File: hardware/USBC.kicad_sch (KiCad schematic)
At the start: 16 parts, among them J20 USB_C_Receptacle_USB2.0_16P, U11 CDSOT236-0504C, U33 USBLC6-2P6, U8 CP2102N-A02-GQFN20

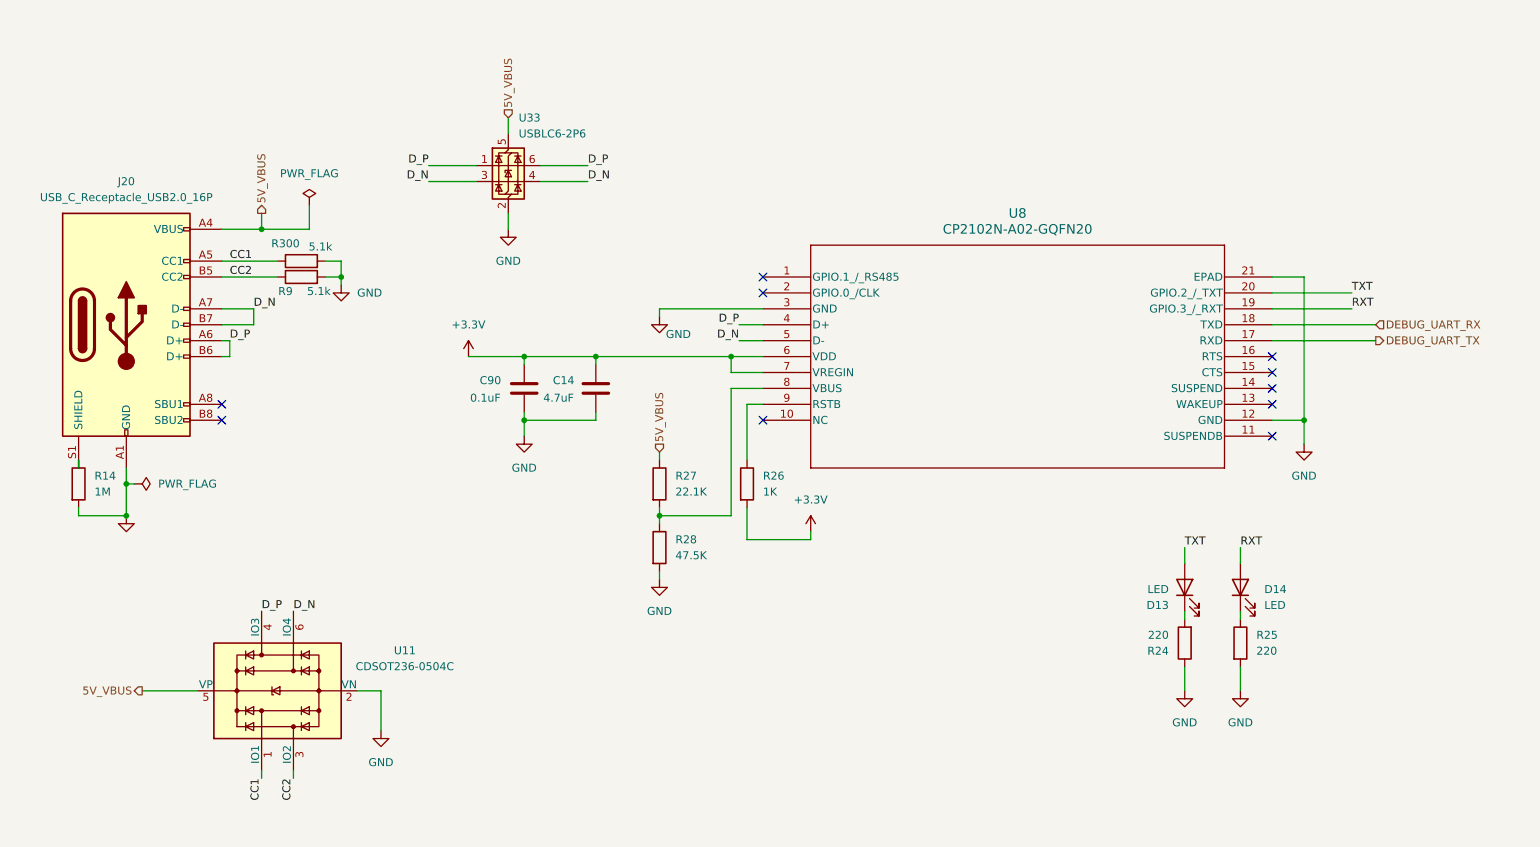
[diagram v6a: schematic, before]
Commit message: updated major symbol and footprints
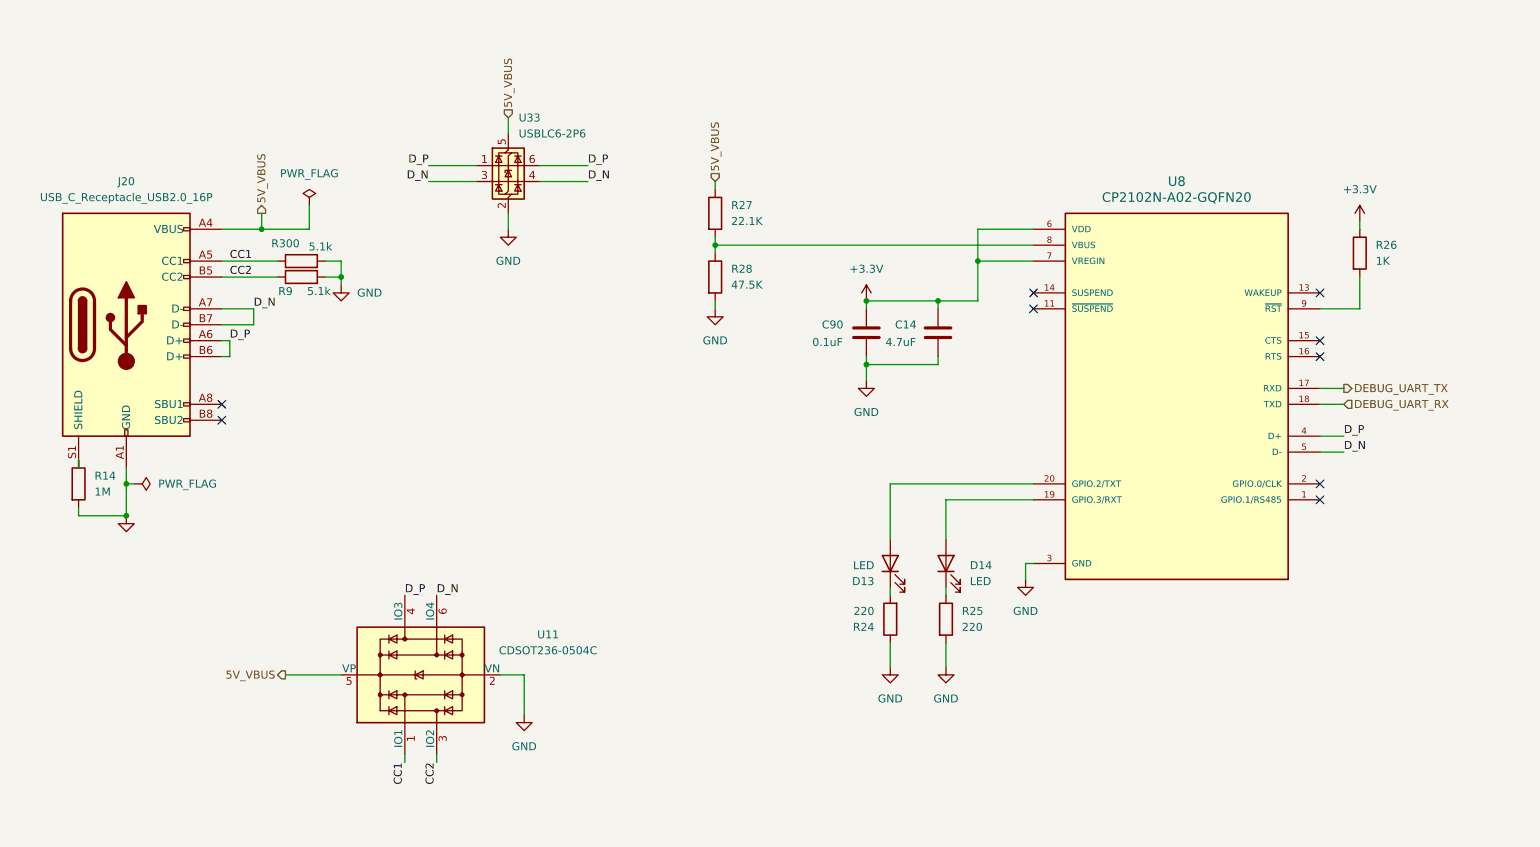
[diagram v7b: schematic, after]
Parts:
- U8: footprint Custom_Parts:QFN50P400X400X80-25N -> pyronet_footprints:SILABS_CP2102N-A02-GQFN20R; symbol 2026-02-15_23-19-28:CP2102N-A02-GQFN20 -> pyronet_symbols:CP2102N-A02-GQFN20R; Availability (none) -> In Stock; Check_prices (none) -> https://www.snapeda.com/parts/CP2102N-A02-GQFN20R/Silicon+L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; Description_1 (none) -> USB Bridge, USB to UART USB 2.0 UART Interface 20-QFN (3x3); MANUFACTURER (none) -> SILICON LABS; MAXIMUM_PACKAGE_HIEGHT (none) -> 0.8mm; MF (none) -> Silicon Labs; MP (none) -> CP2102N-A02-GQFN20R; PARTREV (none) -> 1.3; Package (none) -> WFQFN-20 Silicon Labs; Price (none) -> None; STANDARD (none) -> Manufacturer Recommendations; SnapEDA_Link (none) -> https://www.snapeda.com/parts/CP2102N-A02-GQFN20R/Silicon+L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
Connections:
- net +3.3V: now also R26.1; no longer R26.2
- net at U8.9 (~{RST}): now also R26.2; no longer R26.1
- net RXT: no longer names the net of D14.2 (A), U8.19 (GPIO.3/RXT)
- net TXT: no longer names the net of D13.2 (A), U8.20 (GPIO.2/TXT)
- no-connect marks 10 -> 9
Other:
- moved on the sheet: C14, C90, D13, D14, R24, R25, R26, R27, R28, U11

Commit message: updated 5V power and pin
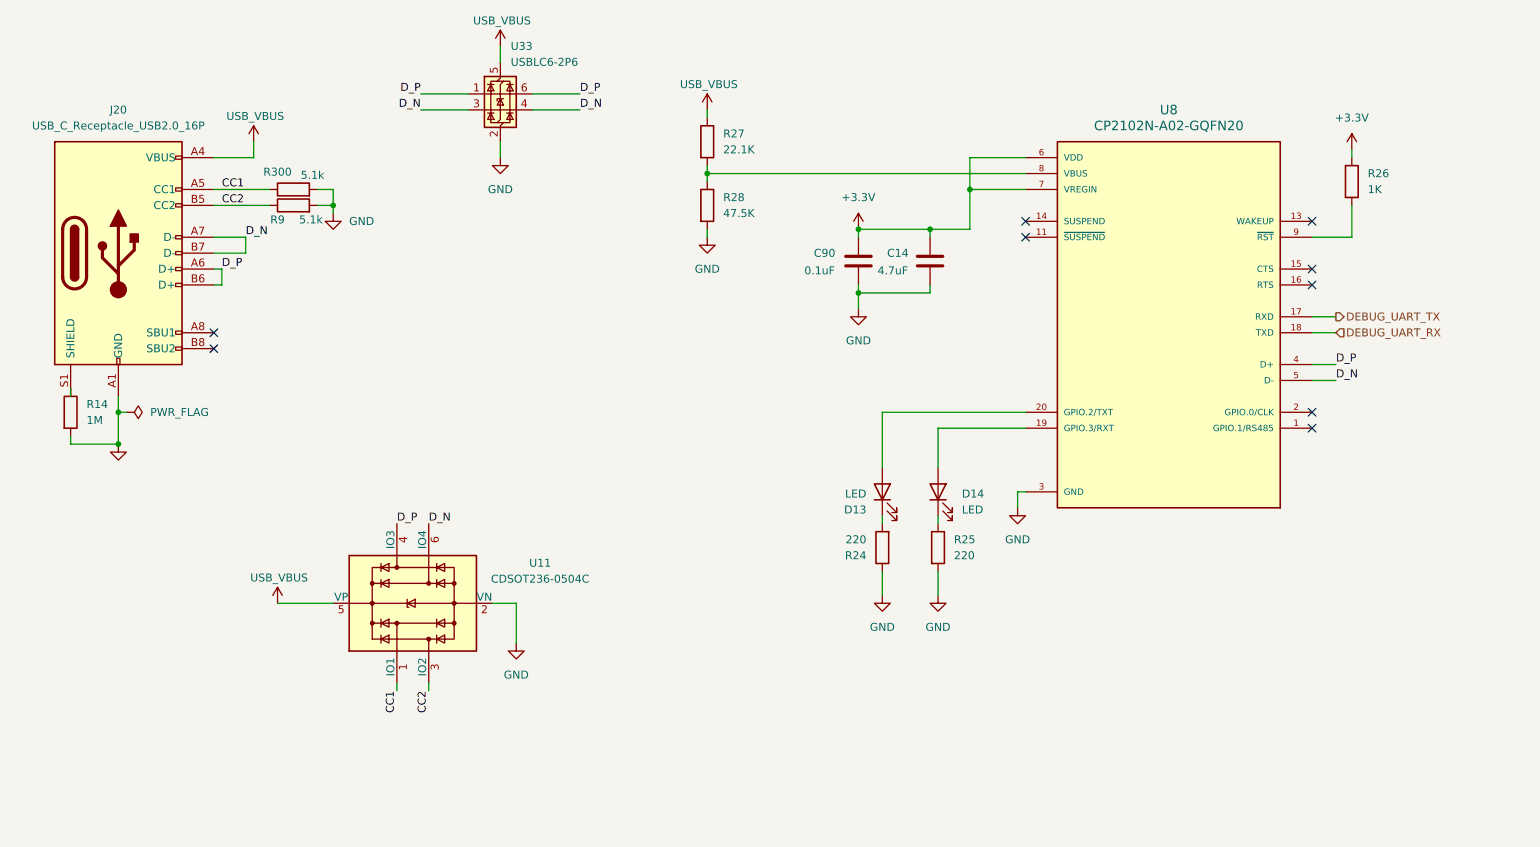
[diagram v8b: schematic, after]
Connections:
- net 5V_VBUS renamed USB_VBUS
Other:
- moved on the sheet: C14, C90, D13, D14, J20, R14, R24, R25, R26, R27, R28, R300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
